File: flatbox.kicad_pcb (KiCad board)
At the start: 2 copper layers, 296 x 196 mm, 39 parts, among them J3 USB_C_Receptacle_USB2.0_16P, SW1 SW_Push, SW10 SW_Push, SW11 SW_Push, SW12 SW_Push, SW13 SW_Push, SW2 SW_Push, SW3 SW_Push, SW4 SW_Push, SW5 SW_Push, SW6 SW_Push, SW7 SW_Push, SW8 SW_Push, SW9 SW_Push, U1 ATmega32U4-A, Y1 16MHz

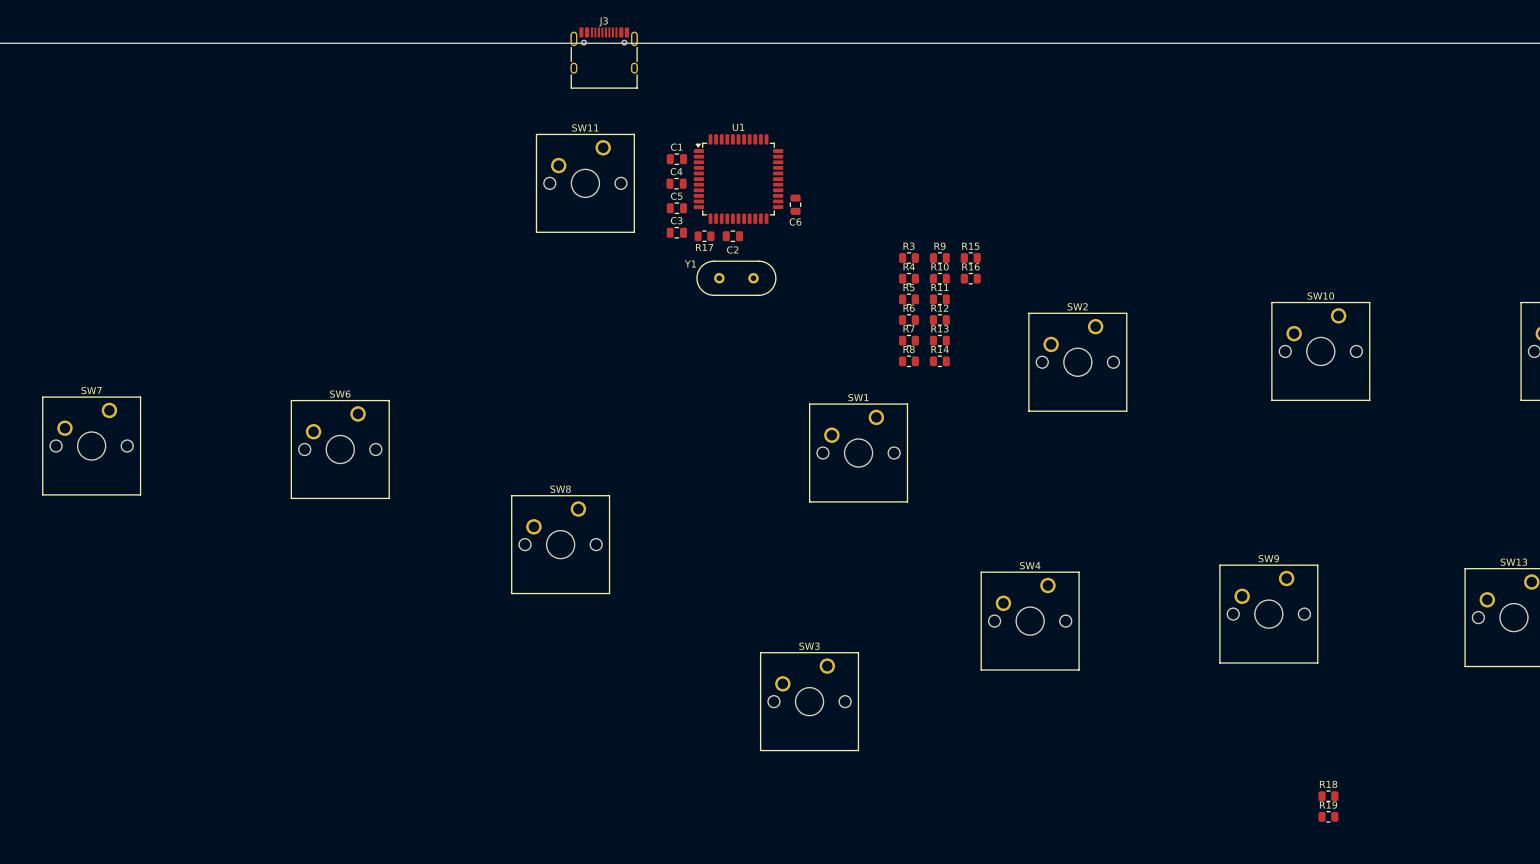
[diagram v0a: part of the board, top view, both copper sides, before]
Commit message: Slight edit to PCB Assembly
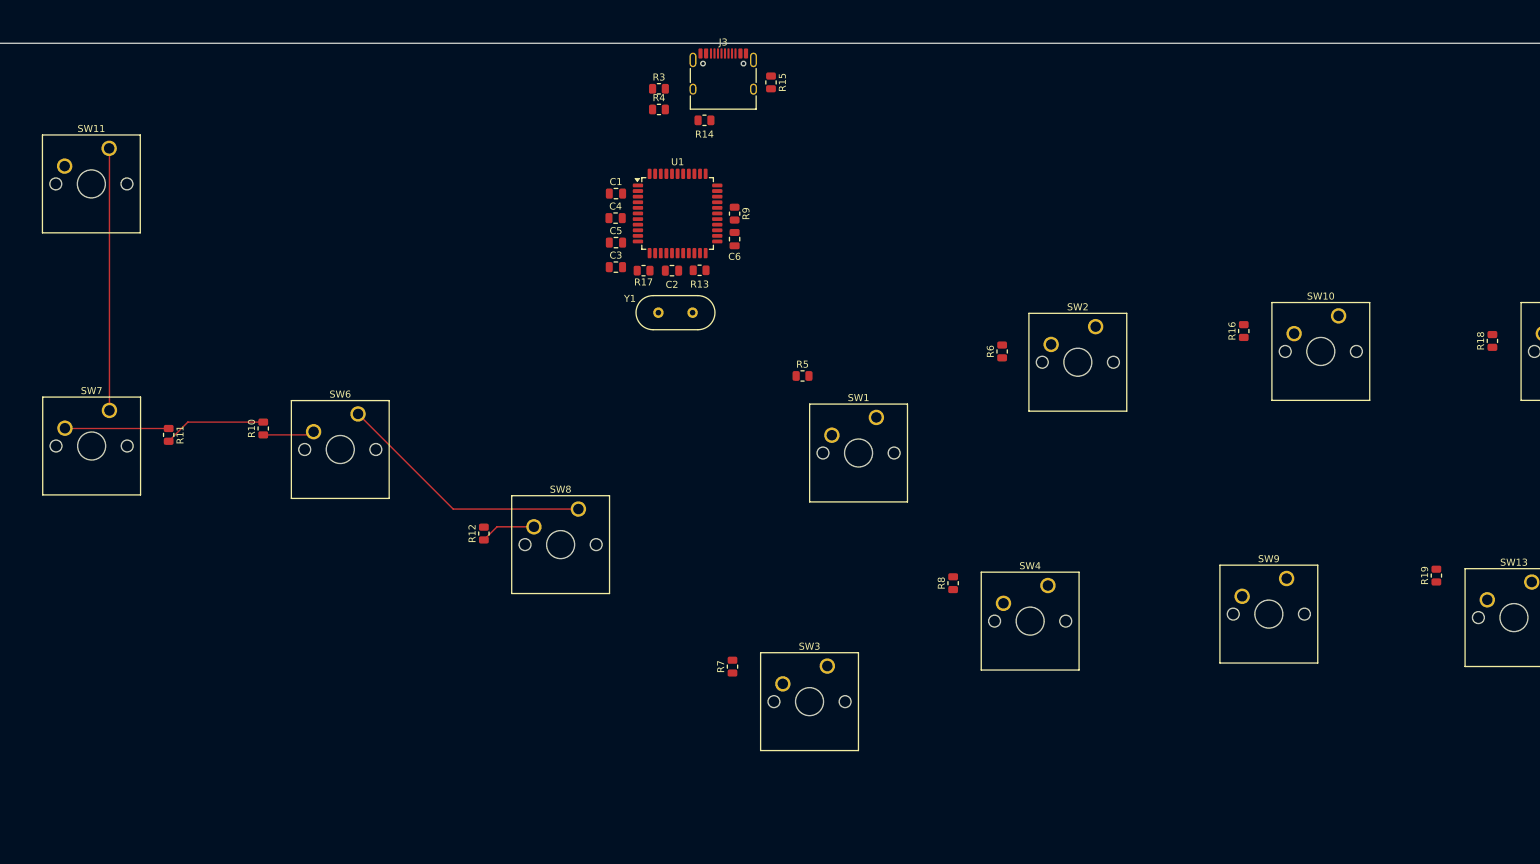
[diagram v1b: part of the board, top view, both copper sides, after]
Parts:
- moved R11 111.8 mm to (114.0, 87.9), turned to -90 degrees
- moved R10 98.9 mm to (127.5, 87.0), turned to 90 degrees
- moved R12 71.9 mm to (159.0, 102.0), turned to 90 degrees
- moved SW11 70.5 mm to (105.5, 47.0)
- moved R18 69.1 mm to (303.0, 74.5), turned to 90 degrees
- moved R7 52.9 mm to (194.5, 121.0), turned to 90 degrees
- moved R14 48.1 mm to (190.5, 43.0)
- moved R3 43.1 mm to (184.0, 38.5)
- moved R4 43.1 mm to (184.0, 41.5)
- moved R16 39.7 mm to (267.5, 73.1), turned to 90 degrees
- moved R15 38.0 mm to (200.0, 37.6), turned to -90 degrees
- moved R19 37.7 mm to (295.0, 108.0), turned to 90 degrees
- moved R13 35.7 mm to (189.8, 64.4), turned to 180 degrees
- moved R8 32.3 mm to (226.0, 109.1), turned to 90 degrees
- moved R9 30.0 mm to (194.8, 56.3), turned to -90 degrees
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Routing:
- net GND: track 0.00 -> 74.5 mm
- net /LEFT: track 0.00 -> 14.8 mm
- net +5V: track 0.00 -> 14.6 mm
- net /RIGHT: track 0.00 -> 7.93 mm
- net /DOWN: track 0.00 -> 7.38 mm
